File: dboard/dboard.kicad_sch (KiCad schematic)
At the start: 17 parts, among them J1 Conn_01x04, U1 TPD2E2U06DRLR, U2 XC6206P332MR

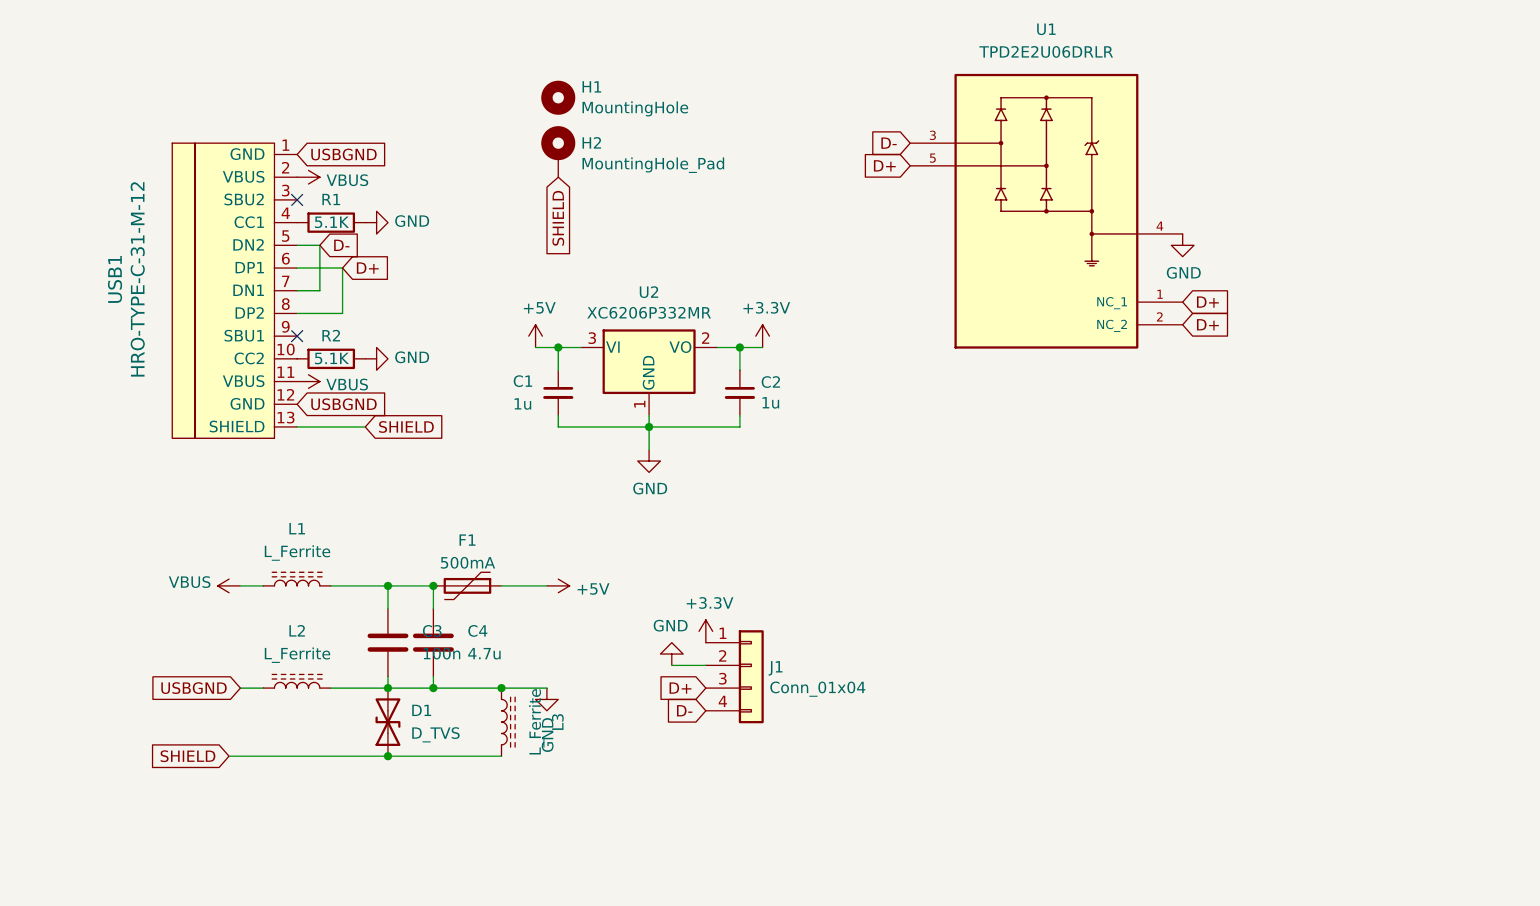
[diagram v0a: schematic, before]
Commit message: added tvs
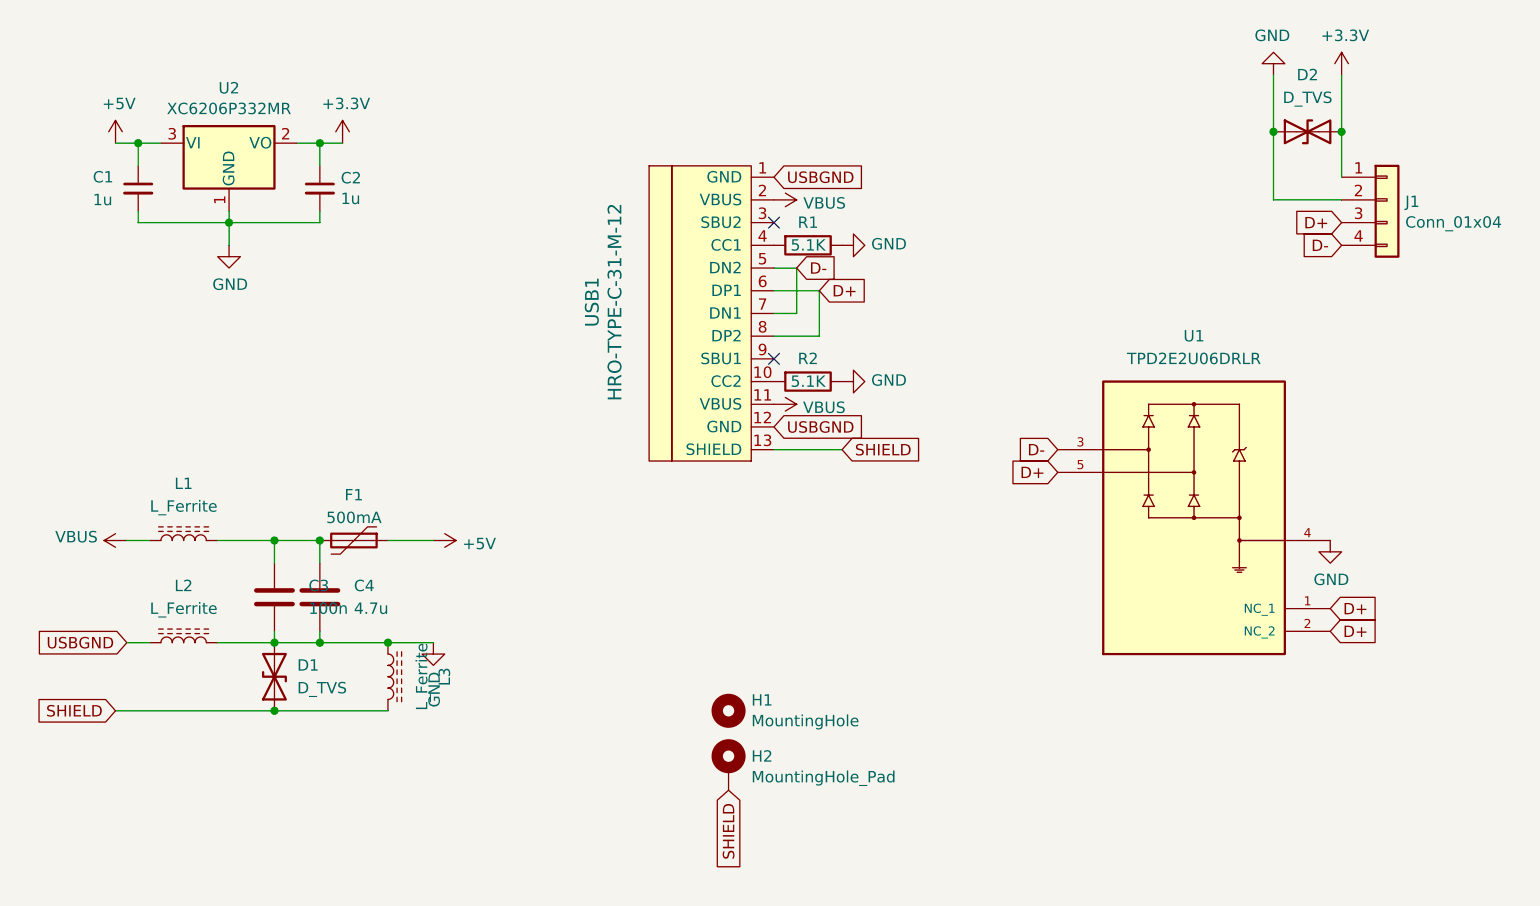
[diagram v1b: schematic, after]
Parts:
- added D2: D_TVS, Diode_SMD:D_SOD-123, symbol Device:D_TVS
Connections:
- net +3V3: now also D2.2 (A2)
- net GND: now also D2.1 (A1)
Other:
- moved on the sheet: C1, C2, C3, C4, D1, F1, H1, H2, J1, L1, L2, L3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

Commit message: rearranged
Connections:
- net GND: now also L2.1, USB1.12 (GND)
- net USBGND: no longer L2.1, USB1.12 (GND)
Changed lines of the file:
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@@
-    )
-  )
-  (global_label "USBGND" (shape input) (at 31.75 93.98 180)
-    (effects (font (size 1.27 1.27)) (justify right))
-    (property "Intersheet References" "${INTERSHEET_REFS}" (id 0) (at 20.1324 94.0594 0)
-      (effects (font (size 1.27 1.27)) (justify right) hide)
     )
   )
@@
     )
   )
-  (global_label "USBGND" (shape input) (at 104.14 69.85 0)
-    (effects (font (size 1.27 1.27)) (justify left))
-    (property "Intersheet References" "${INTERSHEET_REFS}" (id 0) (at 115.7576 69.7706 0)
-      (effects (font (size 1.27 1.27)) (justify left) hide)
-    )
-  )
   (global_label "D-" (shape input) (at 106.68 52.07 0)
     (effects (font (size 1.27 1.27)) (justify left))
@@
     (pin "1")
   )
+  (symbol (lib_id "power:GND") (at 31.75 93.98 270) (unit 1)
+    (in_bom yes) (on_board yes)
+    (property "Reference" "#PWR?" (id 0) (at 25.4 93.98 0)
+      (effects (font (size 1.27 1.27)) hide)
+    )
+    (property "Value" "GND" (id 1) (at 27.3558 94.107 0))
+    (property "Footprint" "" (id 2) (at 31.75 93.98 0)
+      (effects (font (size 1.27 1.27)) hide)
+    )
+    (property "Datasheet" "" (id 3) (at 31.75 93.98 0)
+      (effects (font (size 1.27 1.27)) hide)
+    )
+    (pin "1")
+  )
   (symbol (lib_id "power:GND") (at 43.18 49.53 0) (unit 1)
     (in_bom yes) (on_board yes)
@@
     )
     (property "Datasheet" "" (id 3) (at 66.04 93.98 0)
+      (effects (font (size 1.27 1.27)) hide)
+    )
+    (pin "1")
+  )
+  (symbol (lib_id "power:GND") (at 104.14 69.85 90) (unit 1)
+    (in_bom yes) (on_board yes)
+    (property "Reference" "#PWR?" (id 0) (at 110.49 69.85 0)
+      (effects (font (size 1.27 1.27)) hide)
+    )
+    (property "Value" "GND" (id 1) (at 108.5342 69.723 0))
+    (property "Footprint" "" (id 2) (at 104.14 69.85 0)
+      (effects (font (size 1.27 1.27)) hide)
+    )
+    (property "Datasheet" "" (id 3) (at 104.14 69.85 0)
       (effects (font (size 1.27 1.27)) hide)
     )
@@
       (reference "#PWR0108") (unit 1) (value "GND") (footprint "")
     )
+    (path "/83dc772f-c7be-4e82-8ec5-069f2c2b694e"
+      (reference "#PWR?") (unit 1) (value "GND") (footprint "")
+    )
+    (path "/ef08f82e-b749-4da4-83a9-de2b4476ed58"
+      (reference "#PWR?") (unit 1) (value "GND") (footprint "")
+    )
     (path "/27d80559-e4cf-41a9-911c-b2c54794fb86"

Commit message: curvy
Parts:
- renumbered USB1 to J1, J1 to J2
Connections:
- net USBGND is gone; now on net GND: J1.1 (GND)
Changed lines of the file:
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@@
-    )
-  )
-  (global_label "USBGND" (shape input) (at 104.14 41.91 0)
-    (effects (font (size 1.27 1.27)) (justify left))
-    (property "Intersheet References" "${INTERSHEET_REFS}" (id 0) (at 115.7576 41.8306 0)
-      (effects (font (size 1.27 1.27)) (justify left) hide)
     )
   )
@@
   (symbol (lib_id "power:GND") (at 31.75 93.98 270) (unit 1)
     (in_bom yes) (on_board yes)
-    (property "Reference" "#PWR?" (id 0) (at 25.4 93.98 0)
+    (property "Reference" "#PWR0109" (id 0) (at 25.4 93.98 0)
       (effects (font (size 1.27 1.27)) hide)
     )
@@
     (pin "1")
   )
+  (symbol (lib_id "power:GND") (at 104.14 41.91 90) (unit 1)
+    (in_bom yes) (on_board yes)
+    (property "Reference" "#PWR0110" (id 0) (at 110.49 41.91 0)
+      (effects (font (size 1.27 1.27)) hide)
+    )
+    (property "Value" "GND" (id 1) (at 108.5342 41.783 0))
+    (property "Footprint" "" (id 2) (at 104.14 41.91 0)
+      (effects (font (size 1.27 1.27)) hide)
+    )
+    (property "Datasheet" "" (id 3) (at 104.14 41.91 0)
+      (effects (font (size 1.27 1.27)) hide)
+    )
+    (pin "1")
+  )
   (symbol (lib_id "power:GND") (at 104.14 69.85 90) (unit 1)
     (in_bom yes) (on_board yes)
-    (property "Reference" "#PWR?" (id 0) (at 110.49 69.85 0)
+    (property "Reference" "#PWR0104" (id 0) (at 110.49 69.85 0)
       (effects (font (size 1.27 1.27)) hide)
     )
@@
   (symbol (lib_id "Connector_Generic:Conn_01x04") (at 172.72 44.45 0) (unit 1)
     (in_bom yes) (on_board yes)
-    (property "Reference" "J1" (id 0) (at 174.752 44.6532 0)
+    (property "Reference" "J2" (id 0) (at 174.752 44.653 0)
       (effects (font (size 1.27 1.27)) (justify left))
     )
@@
   (symbol (lib_id "dboard-rescue:HRO-TYPE-C-31-M-12-Type-C") (at 101.6 55.88 0) (unit 1)
     (in_bom yes) (on_board yes)
-    (property "Reference" "USB1" (id 0) (at 83.82 55.88 90)
+    (property "Reference" "J1" (id 0) (at 83.82 55.88 90)
       (effects (font (size 1.524 1.524)))
     )
@@
       (reference "#PWR0103") (unit 1) (value "VBUS") (footprint "")
     )
+    (path "/83dc772f-c7be-4e82-8ec5-069f2c2b694e"
+      (reference "#PWR0104") (unit 1) (value "GND") (footprint "")
+    )
     (path "/58a02a79-1437-4bcc-841d-578eb3577028"
       (reference "#PWR0105") (unit 1) (value "+5V") (footprint "")
@@
       (reference "#PWR0108") (unit 1) (value "GND") (footprint "")
     )
-    (path "/83dc772f-c7be-4e82-8ec5-069f2c2b694e"
-      (reference "#PWR?") (unit 1) (value "GND") (footprint "")
-    )
     (path "/ef08f82e-b749-4da4-83a9-de2b4476ed58"
-      (reference "#PWR?") (unit 1) (value "GND") (footprint "")
+      (reference "#PWR0109") (unit 1) (value "GND") (footprint "")
+    )
+    (path "/e8187c27-f36a-47a1-bf77-83c40a191fdb"
+      (reference "#PWR0110") (unit 1) (value "GND") (footprint "")
     )
     (path "/27d80559-e4cf-41a9-911c-b2c54794fb86"
@@
       (reference "H2") (unit 1) (value "MountingHole_Pad") (footprint "crokto:M3_Via_Hole")
     )
+    (path "/00000000-0000-0000-0000-00005feaf32e"
+      (reference "J1") (unit 1) (value "HRO-TYPE-C-31-M-12") (footprint "Type-C:HRO-TYPE-C-31-M-12-Assembly")
+    )
     (path "/00000000-0000-0000-0000-00005fec6f34"
-      (reference "J1") (unit 1) (value "Conn_01x04") (footprint "crokto:JST_SH_SM04B-SRSS-TB_1x04-1MP_P1.00mm_Horizontal")
+      (reference "J2") (unit 1) (value "Conn_01x04") (footprint "crokto:JST_SH_SM04B-SRSS-TB_1x04-1MP_P1.00mm_Horizontal")
     )
     (path "/b456c4a2-2574-41d8-bfe0-074db91178da"
@@
       (reference "U2") (unit 1) (value "XC6206P332MR") (footprint "Package_TO_SOT_SMD:SOT-23")
     )
-    (path "/00000000-0000-0000-0000-00005feaf32e"
-      (reference "USB1") (unit 1) (value "HRO-TYPE-C-31-M-12") (footprint "Type-C:HRO-TYPE-C-31-M-12-Assembly")
-    )
-  )
+  )

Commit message: changes
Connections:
- net +3V3: no longer D2.2 (A2)
- net +5V: now also D2.2 (A2)
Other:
- moved on the sheet: D2
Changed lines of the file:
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@@
   (junction (at 53.34 93.98) (diameter 0.9144) (color 0 0 0 0))
   (junction (at 60.96 93.98) (diameter 0.9144) (color 0 0 0 0))
-  (junction (at 160.02 36.83) (diameter 0.9144) (color 0 0 0 0))
-  (junction (at 167.64 36.83) (diameter 0.9144) (color 0 0 0 0))
+  (junction (at 64.77 82.55) (diameter 0.9144) (color 0 0 0 0))
+  (junction (at 64.77 93.98) (diameter 0.9144) (color 0 0 0 0))
   (no_connect (at 104.14 46.99))
   (no_connect (at 104.14 62.23))
@@
     (stroke (width 0) (type solid) (color 0 0 0 0))
   )
-  (wire (pts (xy 60.96 82.55) (xy 66.04 82.55))
-    (stroke (width 0) (type solid) (color 0 0 0 0))
-  )
-  (wire (pts (xy 60.96 93.98) (xy 66.04 93.98))
+  (wire (pts (xy 60.96 82.55) (xy 64.77 82.55))
+    (stroke (width 0) (type solid) (color 0 0 0 0))
+  )
+  (wire (pts (xy 60.96 93.98) (xy 64.77 93.98))
+    (stroke (width 0) (type solid) (color 0 0 0 0))
+  )
+  (wire (pts (xy 64.77 82.55) (xy 66.04 82.55))
+    (stroke (width 0) (type solid) (color 0 0 0 0))
+  )
+  (wire (pts (xy 64.77 90.17) (xy 64.77 93.98))
+    (stroke (width 0) (type solid) (color 0 0 0 0))
+  )
+  (wire (pts (xy 64.77 93.98) (xy 66.04 93.98))
     (stroke (width 0) (type solid) (color 0 0 0 0))
   )
@@
     (stroke (width 0) (type solid) (color 0 0 0 0))
   )
-  (wire (pts (xy 160.02 30.48) (xy 160.02 36.83))
-    (stroke (width 0) (type solid) (color 0 0 0 0))
-  )
-  (wire (pts (xy 160.02 36.83) (xy 160.02 44.45))
+  (wire (pts (xy 160.02 30.48) (xy 160.02 44.45))
     (stroke (width 0) (type solid) (color 0 0 0 0))
   )
@@
     (stroke (width 0) (type solid) (color 0 0 0 0))
   )
-  (wire (pts (xy 167.64 30.48) (xy 167.64 36.83))
-    (stroke (width 0) (type solid) (color 0 0 0 0))
-  )
-  (wire (pts (xy 167.64 36.83) (xy 167.64 41.91))
+  (wire (pts (xy 167.64 30.48) (xy 167.64 41.91))
     (stroke (width 0) (type solid) (color 0 0 0 0))
   )
@@
     (pin "2")
   )
-  (symbol (lib_id "Device:D_TVS") (at 163.83 36.83 0) (unit 1)
-    (in_bom yes) (on_board yes)
-    (property "Reference" "D2" (id 0) (at 163.83 30.48 0))
-    (property "Value" "D_TVS" (id 1) (at 163.83 33.02 0))
-    (property "Footprint" "Diode_SMD:D_SOD-123" (id 2) (at 163.83 36.83 0)
-      (effects (font (size 1.27 1.27)) hide)
-    )
-    (property "Datasheet" "~" (id 3) (at 163.83 36.83 0)
-      (effects (font (size 1.27 1.27)) hide)
-    )
+  (symbol (lib_id "Device:D_TVS") (at 64.77 86.36 90) (unit 1)
+    (in_bom yes) (on_board yes)
+    (property "Reference" "D2" (id 0) (at 58.42 86.36 0))
+    (property "Value" "D_TVS" (id 1) (at 60.96 86.36 0))
+    (property "Footprint" "Diode_SMD:D_SOD-123" (id 2) (at 64.77 86.36 0)
+      (effects (font (size 1.27 1.27)) hide)
+    )
+    (property "Datasheet" "~" (id 3) (at 64.77 86.36 0)
+      (effects (font (size 1.27 1.27)) hide)
+    )
